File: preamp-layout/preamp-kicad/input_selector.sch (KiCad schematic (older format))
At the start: 40 parts, among them J50 Conn_01x03_Female, J51 Conn_01x03_Male, J52 Conn_01x03_Male, J53 Conn_01x03_Male, J54 Conn_01x03_Male, J55 Conn_01x07_Female, J56 Conn_01x07_Female, J57 Conn_01x03_Male, J58 Conn_01x03_Male, J59 Conn_01x03_Female, J60 Conn_01x02_Male, J61 Conn_01x02_Male, J62 Conn_01x03_Female, J63 Conn_01x03_Female, K2 G6JU, K3 G6JU, K4 G6JU, K5 G6JU, K6 G6JU, K7 G6JU, K8 G6JU, U6 MCP23S17_SP, U7 ULN2003, U8 ULN2003

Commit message: Footprint updates
Footprint creation of relay, ESP32
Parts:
- K2, K3, K4, K5, K6, K7, K8: footprint (none) -> preamp:Relay_DPDT_Omron_G6JU-2P-Y
- U6: footprint Package_DIP:DIP-28_W7.62mm -> Package_SO:SOIC-28W_7.5x17.9mm_P1.27mm
- U7, U8: footprint (none) -> Package_SO:SOIC-16_3.9x9.9mm_P1.27mm
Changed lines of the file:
@@
 F 0 "U8" H 4900 4067 50  0000 C CNN
 F 1 "ULN2003" H 4900 3976 50  0000 C CNN
-F 2 "" H 4950 2850 50  0001 L CNN
+F 2 "Package_SO:SOIC-16_3.9x9.9mm_P1.27mm" H 4950 2850 50  0001 L CNN
 F 3 "http://www.ti.com/lit/ds/symlink/uln2003a.pdf" H 5000 3200 50  0001 C CNN
 	1    4900 3400
@@
 F 0 "U7" H 4900 2267 50  0000 C CNN
 F 1 "ULN2003" H 4900 2176 50  0000 C CNN
-F 2 "" H 4950 1050 50  0001 L CNN
+F 2 "Package_SO:SOIC-16_3.9x9.9mm_P1.27mm" H 4950 1050 50  0001 L CNN
 F 3 "http://www.ti.com/lit/ds/symlink/uln2003a.pdf" H 5000 1400 50  0001 C CNN
 	1    4900 1600
@@
 F 0 "K2" V 10304 1928 50  0000 L CNN
 F 1 "G6JU" V 10395 1928 50  0000 L CNN
-F 2 "" H 10350 1850 50  0001 C CNN
+F 2 "preamp:Relay_DPDT_Omron_G6JU-2P-Y" H 10350 1850 50  0001 C CNN
 F 3 "https://omronfs.omron.com/en_US/ecb/products/pdf/en-g6j.pdf" H 10350 1850 50  0001 C CNN
 	1    10350 1750
@@
 F 0 "K3" V 10304 2928 50  0000 L CNN
 F 1 "G6JU" V 10395 2928 50  0000 L CNN
-F 2 "" H 10350 2850 50  0001 C CNN
+F 2 "preamp:Relay_DPDT_Omron_G6JU-2P-Y" H 10350 2850 50  0001 C CNN
 F 3 "https://omronfs.omron.com/en_US/ecb/products/pdf/en-g6j.pdf" H 10350 2850 50  0001 C CNN
 	1    10350 2750
@@
 F 0 "K4" V 10304 3928 50  0000 L CNN
 F 1 "G6JU" V 10395 3928 50  0000 L CNN
-F 2 "" H 10350 3850 50  0001 C CNN
+F 2 "preamp:Relay_DPDT_Omron_G6JU-2P-Y" H 10350 3850 50  0001 C CNN
 F 3 "https://omronfs.omron.com/en_US/ecb/products/pdf/en-g6j.pdf" H 10350 3850 50  0001 C CNN
 	1    10350 3750
@@
 F 0 "K5" V 10304 4928 50  0000 L CNN
 F 1 "G6JU" V 10395 4928 50  0000 L CNN
-F 2 "" H 10350 4850 50  0001 C CNN
+F 2 "preamp:Relay_DPDT_Omron_G6JU-2P-Y" H 10350 4850 50  0001 C CNN
 F 3 "https://omronfs.omron.com/en_US/ecb/products/pdf/en-g6j.pdf" H 10350 4850 50  0001 C CNN
 	1    10350 4750
@@
 F 0 "K6" V 10304 5928 50  0000 L CNN
 F 1 "G6JU" V 10395 5928 50  0000 L CNN
-F 2 "" H 10350 5850 50  0001 C CNN
+F 2 "preamp:Relay_DPDT_Omron_G6JU-2P-Y" H 10350 5850 50  0001 C CNN
 F 3 "https://omronfs.omron.com/en_US/ecb/products/pdf/en-g6j.pdf" H 10350 5850 50  0001 C CNN
 	1    10350 5750
@@
 F 0 "K7" V 8604 1878 50  0000 L CNN
 F 1 "G6JU" V 8695 1878 50  0000 L CNN
-F 2 "" H 8650 1800 50  0001 C CNN
+F 2 "preamp:Relay_DPDT_Omron_G6JU-2P-Y" H 8650 1800 50  0001 C CNN
 F 3 "https://omronfs.omron.com/en_US/ecb/products/pdf/en-g6j.pdf" H 8650 1800 50  0001 C CNN
 	1    8650 1700
@@
 F 0 "K8" V 8604 2878 50  0000 L CNN
 F 1 "G6JU" V 8695 2878 50  0000 L CNN
-F 2 "" H 8650 2800 50  0001 C CNN
+F 2 "preamp:Relay_DPDT_Omron_G6JU-2P-Y" H 8650 2800 50  0001 C CNN
 F 3 "https://omronfs.omron.com/en_US/ecb/products/pdf/en-g6j.pdf" H 8650 2800 50  0001 C CNN
 	1    8650 2700
@@
 F 0 "K8" H 8550 5727 50  0000 C CNN
 F 1 "G6JU" H 8550 5636 50  0000 C CNN
-F 2 "" H 8550 6050 50  0001 C CNN
+F 2 "preamp:Relay_DPDT_Omron_G6JU-2P-Y" H 8550 6050 50  0001 C CNN
 F 3 "https://omronfs.omron.com/en_US/ecb/products/pdf/en-g6j.pdf" H 8550 6050 50  0001 C CNN
 	3    8550 5950
@@
 F 0 "K8" H 8550 5675 50  0000 C CNN
 F 1 "G6JU" H 8550 5584 50  0000 C CNN
-F 2 "" H 8550 5450 50  0001 C CNN
+F 2 "preamp:Relay_DPDT_Omron_G6JU-2P-Y" H 8550 5450 50  0001 C CNN
 F 3 "https://omronfs.omron.com/en_US/ecb/products/pdf/en-g6j.pdf" H 8550 5450 50  0001 C CNN
 	2    8550 5350
@@
 F 0 "K7" H 8550 4277 50  0000 C CNN
 F 1 "G6JU" H 8550 4186 50  0000 C CNN
-F 2 "" H 8550 4600 50  0001 C CNN
+F 2 "preamp:Relay_DPDT_Omron_G6JU-2P-Y" H 8550 4600 50  0001 C CNN
 F 3 "https://omronfs.omron.com/en_US/ecb/products/pdf/en-g6j.pdf" H 8550 4600 50  0001 C CNN
 	3    8550 4500
@@
 F 0 "K7" H 8550 4225 50  0000 C CNN
 F 1 "G6JU" H 8550 4134 50  0000 C CNN
-F 2 "" H 8550 4000 50  0001 C CNN
+F 2 "preamp:Relay_DPDT_Omron_G6JU-2P-Y" H 8550 4000 50  0001 C CNN
 F 3 "https://omronfs.omron.com/en_US/ecb/products/pdf/en-g6j.pdf" H 8550 4000 50  0001 C CNN
 	2    8550 3900
@@
 F 0 "K2" H 1950 5277 50  0000 C CNN
 F 1 "G6JU" H 1950 5186 50  0000 C CNN
-F 2 "" H 1950 5600 50  0001 C CNN
+F 2 "preamp:Relay_DPDT_Omron_G6JU-2P-Y" H 1950 5600 50  0001 C CNN
 F 3 "https://omronfs.omron.com/en_US/ecb/products/pdf/en-g6j.pdf" H 1950 5600 50  0001 C CNN
 	3    1950 5500
@@
 F 0 "K2" H 1950 5225 50  0000 C CNN
 F 1 "G6JU" H 1950 5134 50  0000 C CNN
-F 2 "" H 1950 5000 50  0001 C CNN
+F 2 "preamp:Relay_DPDT_Omron_G6JU-2P-Y" H 1950 5000 50  0001 C CNN
 F 3 "https://omronfs.omron.com/en_US/ecb/products/pdf/en-g6j.pdf" H 1950 5000 50  0001 C CNN
 	2    1950 4900
@@
 F 0 "K3" H 3750 5277 50  0000 C CNN
 F 1 "G6JU" H 3750 5186 50  0000 C CNN
-F 2 "" H 3750 5600 50  0001 C CNN
+F 2 "preamp:Relay_DPDT_Omron_G6JU-2P-Y" H 3750 5600 50  0001 C CNN
 F 3 "https://omronfs.omron.com/en_US/ecb/products/pdf/en-g6j.pdf" H 3750 5600 50  0001 C CNN
 	3    3750 5500
@@
 F 0 "K3" H 3750 5225 50  0000 C CNN
 F 1 "G6JU" H 3750 5134 50  0000 C CNN
-F 2 "" H 3750 5000 50  0001 C CNN
+F 2 "preamp:Relay_DPDT_Omron_G6JU-2P-Y" H 3750 5000 50  0001 C CNN
 F 3 "https://omronfs.omron.com/en_US/ecb/products/pdf/en-g6j.pdf" H 3750 5000 50  0001 C CNN
 	2    3750 4900
@@
 F 0 "K4" H 1950 6927 50  0000 C CNN
 F 1 "G6JU" H 1950 6836 50  0000 C CNN
-F 2 "" H 1950 7250 50  0001 C CNN
+F 2 "preamp:Relay_DPDT_Omron_G6JU-2P-Y" H 1950 7250 50  0001 C CNN
 F 3 "https://omronfs.omron.com/en_US/ecb/products/pdf/en-g6j.pdf" H 1950 7250 50  0001 C CNN
 	3    1950 7150
@@
 F 0 "K5" H 3750 6927 50  0000 C CNN
 F 1 "G6JU" H 3750 6836 50  0000 C CNN
-F 2 "" H 3750 7250 50  0001 C CNN
+F 2 "preamp:Relay_DPDT_Omron_G6JU-2P-Y" H 3750 7250 50  0001 C CNN
 F 3 "https://omronfs.omron.com/en_US/ecb/products/pdf/en-g6j.pdf" H 3750 7250 50  0001 C CNN
 	3    3750 7150
@@
 F 0 "K5" H 3750 6875 50  0000 C CNN
 F 1 "G6JU" H 3750 6784 50  0000 C CNN
-F 2 "" H 3750 6650 50  0001 C CNN
+F 2 "preamp:Relay_DPDT_Omron_G6JU-2P-Y" H 3750 6650 50  0001 C CNN
 F 3 "https://omronfs.omron.com/en_US/ecb/products/pdf/en-g6j.pdf" H 3750 6650 50  0001 C CNN
 	2    3750 6550
@@
 F 0 "K6" H 5550 6927 50  0000 C CNN
 F 1 "G6JU" H 5550 6836 50  0000 C CNN
-F 2 "" H 5550 7250 50  0001 C CNN
+F 2 "preamp:Relay_DPDT_Omron_G6JU-2P-Y" H 5550 7250 50  0001 C CNN
 F 3 "https://omronfs.omron.com/en_US/ecb/products/pdf/en-g6j.pdf" H 5550 7250 50  0001 C CNN
 	3    5550 7150
@@
 F 0 "K6" H 5550 6875 50  0000 C CNN
 F 1 "G6JU" H 5550 6784 50  0000 C CNN
-F 2 "" H 5550 6650 50  0001 C CNN
+F 2 "preamp:Relay_DPDT_Omron_G6JU-2P-Y" H 5550 6650 50  0001 C CNN
 F 3 "https://omronfs.omron.com/en_US/ecb/products/pdf/en-g6j.pdf" H 5550 6650 50  0001 C CNN
 	2    5550 6550
@@
 F 0 "K4" H 1950 6875 50  0000 C CNN
 F 1 "G6JU" H 1950 6784 50  0000 C CNN
-F 2 "" H 1950 6650 50  0001 C CNN
+F 2 "preamp:Relay_DPDT_Omron_G6JU-2P-Y" H 1950 6650 50  0001 C CNN
 F 3 "https://omronfs.omron.com/en_US/ecb/products/pdf/en-g6j.pdf" H 1950 6650 50  0001 C CNN
 	2    1950 6550
@@
 F 0 "U6" H 2500 3800 50  0000 C CNN
 F 1 "MCP23S17_SP" H 2500 3700 50  0000 C CNN
-F 2 "Package_DIP:DIP-28_W7.62mm" H 2400 1700 50  0001 L CNN
+F 2 "Package_SO:SOIC-28W_7.5x17.9mm_P1.27mm" H 2400 1700 50  0001 L CNN
 F 3 "http://ww1.microchip.com/downloads/en/DeviceDoc/20001952C.pdf" H 2400 1600 50  0001 L CNN
 	1    2200 2700
@@
 P 7000 3150
 AR Path="/6009D432/60248FFE" Ref="#PWR?"  Part="1"
-AR Path="/5E2D8DA2/60248FFE" Ref="#PWR?"  Part="1"
-F 0 "#PWR?" H 7000 2900 50  0001 C CNN
+AR Path="/5E2D8DA2/60248FFE" Ref="#PWR0101"  Part="1"
+F 0 "#PWR0101" H 7000 2900 50  0001 C CNN
 F 1 "GND" H 7005 2977 50  0000 C CNN
 F 2 "" H 7000 3150 50  0001 C CNN

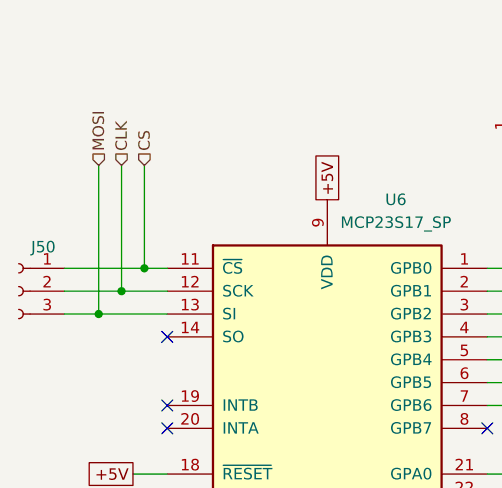
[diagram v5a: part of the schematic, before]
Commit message: Conn / Pin Updates
Updated cable headers, pin names, MCU conn layout. MCP4902 changeout for custom symbol.
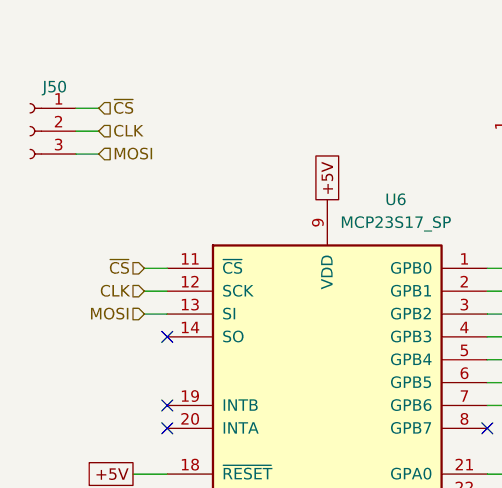
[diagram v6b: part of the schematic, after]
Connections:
- net CS renamed ~CS
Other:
- moved on the sheet: J50
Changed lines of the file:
@@
 Wire Wire Line
 	7000 2050 7000 2150
-Text HLabel 1300 1450 1    50   Input ~ 0
+Text HLabel 1400 2000 0    50   Input ~ 0
 CLK
-Text HLabel 1400 1450 1    50   Input ~ 0
-CS
-Text HLabel 1200 1450 1    50   Input ~ 0
+Text HLabel 1400 1900 0    50   Input ~ 0
+~CS
+Text HLabel 1400 2100 0    50   Input ~ 0
 MOSI
-Wire Wire Line
-	1050 1900 1400 1900
-Wire Wire Line
-	1050 2100 1200 2100
-Wire Wire Line
-	1200 1450 1200 2100
 Text Label 5550 1900 0    50   ~ 0
 IN_3_R+
@@
 L Connector:Conn_01x03_Female J?
 U 1 1 6152C395
-P 850 2000
+P 900 1300
 AR Path="/5E607732/6152C395" Ref="J?"  Part="1"
 AR Path="/5E2D8DA2/6152C395" Ref="J50"  Part="1"
-F 0 "J50" H 742 2193 50  0000 C CNN
-F 1 "Conn_01x03_Female" H 878 1935 50  0001 L CNN
-F 2 "Connector_PinHeader_2.54mm:PinHeader_1x03_P2.54mm_Vertical" H 850 2000 50  0001 C CNN
-F 3 "~" H 850 2000 50  0001 C CNN
-	1    850  2000
+F 0 "J50" H 792 1493 50  0000 C CNN
+F 1 "Conn_01x03_Female" H 928 1235 50  0001 L CNN
+F 2 "Connector_PinHeader_2.54mm:PinHeader_1x03_P2.54mm_Vertical" H 900 1300 50  0001 C CNN
+F 3 "~" H 900 1300 50  0001 C CNN
+	1    900  1300
 	-1   0    0    -1
 $EndComp
@@
 	1    0    0    -1
 $EndComp
-Wire Wire Line
-	1050 2000 1300 2000
-Wire Wire Line
-	1300 1450 1300 2000
-Wire Wire Line
-	1400 1450 1400 1900
-Connection ~ 1200 2100
-Connection ~ 1300 2000
-Connection ~ 1400 1900
-Wire Wire Line
-	1400 1900 1500 1900
-Wire Wire Line
-	1200 2100 1500 2100
-Wire Wire Line
-	1300 2000 1500 2000
 Text GLabel 7000 2850 1    50   UnSpc ~ 0
 +5V
@@
 Wire Wire Line
 	7000 2950 6900 2950
+Wire Wire Line
+	1100 1200 1200 1200
+Wire Wire Line
+	1100 1300 1200 1300
+Wire Wire Line
+	1100 1400 1200 1400
+Wire Wire Line
+	1500 1900 1400 1900
+Wire Wire Line
+	1500 2000 1400 2000
+Wire Wire Line
+	1500 2100 1400 2100
+Text HLabel 1200 1300 2    50   Input ~ 0
+CLK
+Text HLabel 1200 1200 2    50   Input ~ 0
+~CS
+Text HLabel 1200 1400 2    50   Input ~ 0
+MOSI
 $EndSCHEMATC

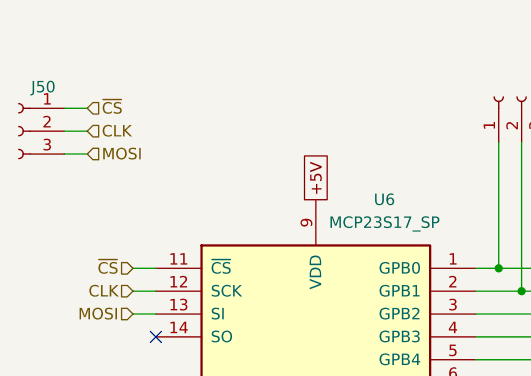
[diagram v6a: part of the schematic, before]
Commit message: Power Supply Update
Grounding made more clear, tied to chassis on AC board. Pins renamed. Aligned with AC wall power convention. General cleanup.
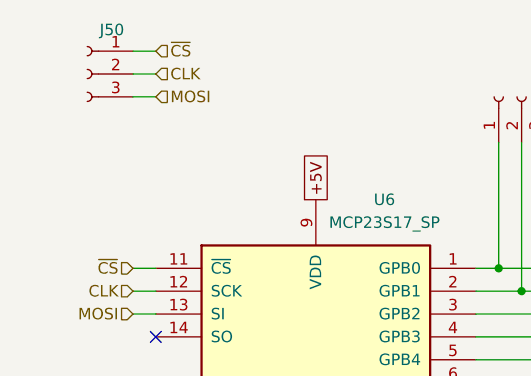
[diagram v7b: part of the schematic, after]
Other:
- moved on the sheet: J50
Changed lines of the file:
@@
 L Connector:Conn_01x03_Female J?
 U 1 1 6152C395
-P 900 1300
+P 1200 1050
 AR Path="/5E607732/6152C395" Ref="J?"  Part="1"
 AR Path="/5E2D8DA2/6152C395" Ref="J50"  Part="1"
-F 0 "J50" H 792 1493 50  0000 C CNN
-F 1 "Conn_01x03_Female" H 928 1235 50  0001 L CNN
-F 2 "Connector_PinHeader_2.54mm:PinHeader_1x03_P2.54mm_Vertical" H 900 1300 50  0001 C CNN
-F 3 "~" H 900 1300 50  0001 C CNN
-	1    900  1300
+F 0 "J50" H 1092 1243 50  0000 C CNN
+F 1 "Conn_01x03_Female" H 1228 985 50  0001 L CNN
+F 2 "Connector_PinHeader_2.54mm:PinHeader_1x03_P2.54mm_Vertical" H 1200 1050 50  0001 C CNN
+F 3 "~" H 1200 1050 50  0001 C CNN
+	1    1200 1050
 	-1   0    0    -1
 $EndComp
@@
 	7000 2950 6900 2950
 Wire Wire Line
-	1100 1200 1200 1200
-Wire Wire Line
-	1100 1300 1200 1300
-Wire Wire Line
-	1100 1400 1200 1400
+	1400 950  1500 950
+Wire Wire Line
+	1400 1050 1500 1050
+Wire Wire Line
+	1400 1150 1500 1150
 Wire Wire Line
 	1500 1900 1400 1900
@@
 Wire Wire Line
 	1500 2100 1400 2100
-Text HLabel 1200 1300 2    50   Input ~ 0
+Text HLabel 1500 1050 2    50   Input ~ 0
 CLK
-Text HLabel 1200 1200 2    50   Input ~ 0
+Text HLabel 1500 950  2    50   Input ~ 0
 ~CS
-Text HLabel 1200 1400 2    50   Input ~ 0
+Text HLabel 1500 1150 2    50   Input ~ 0
 MOSI
 $EndSCHEMATC

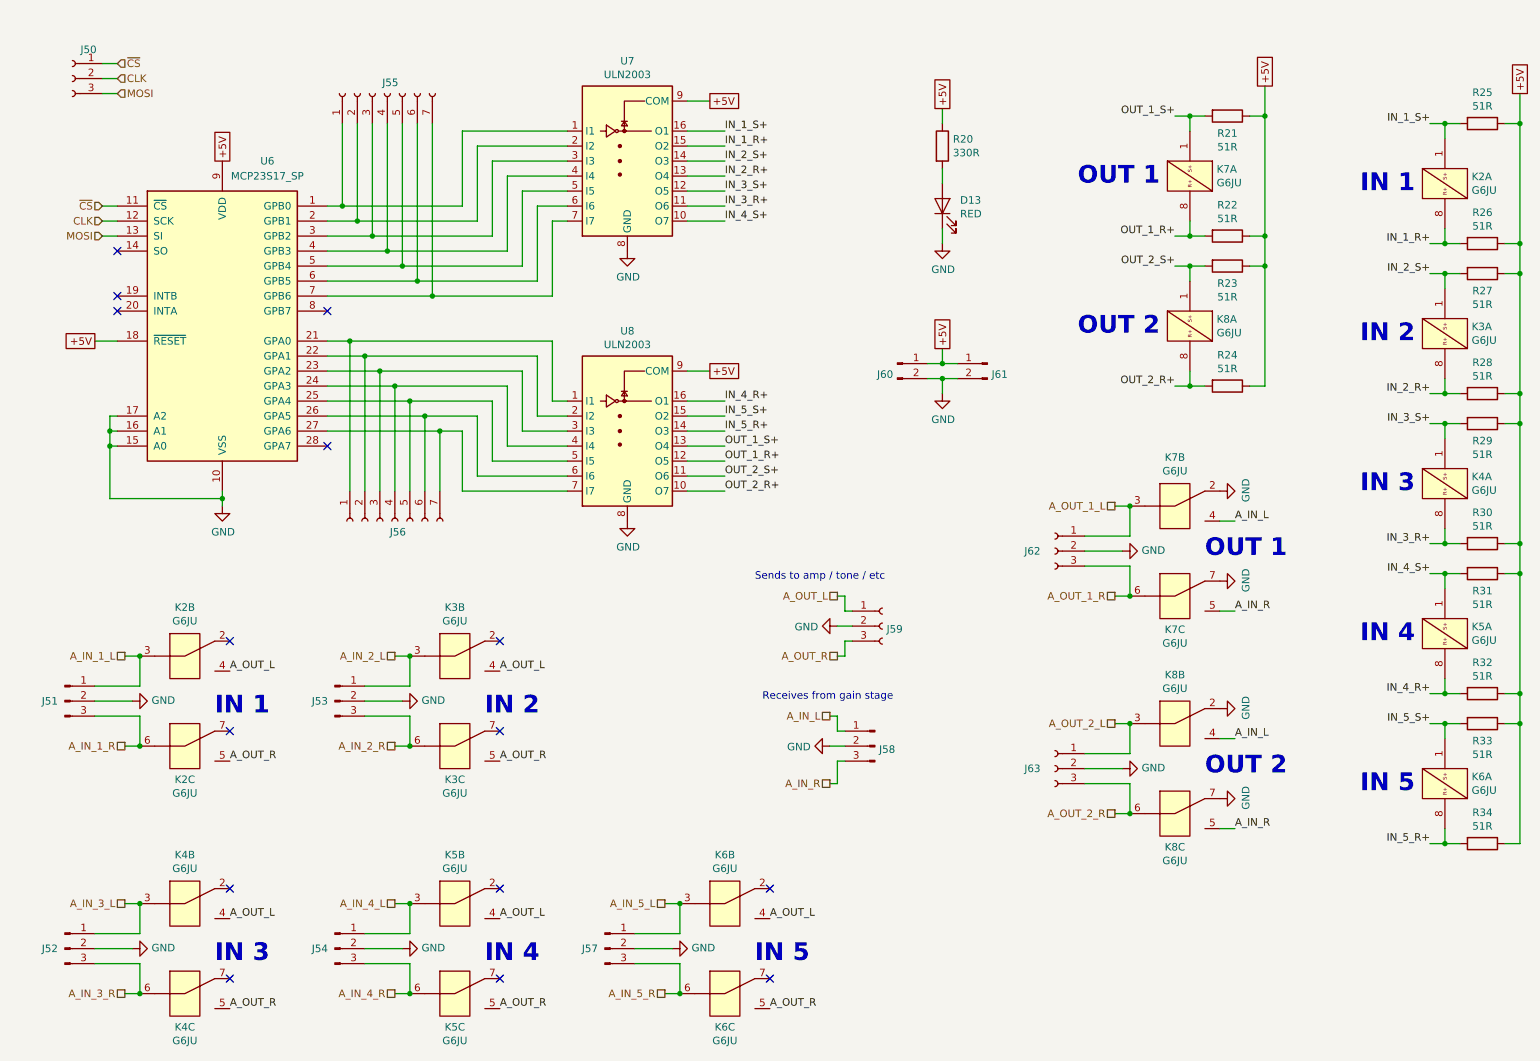
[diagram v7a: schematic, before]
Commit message: Schematic layout updates
schematic optimization. Also implemented encoders with surrounding circuitry (self-contained on encoder board)
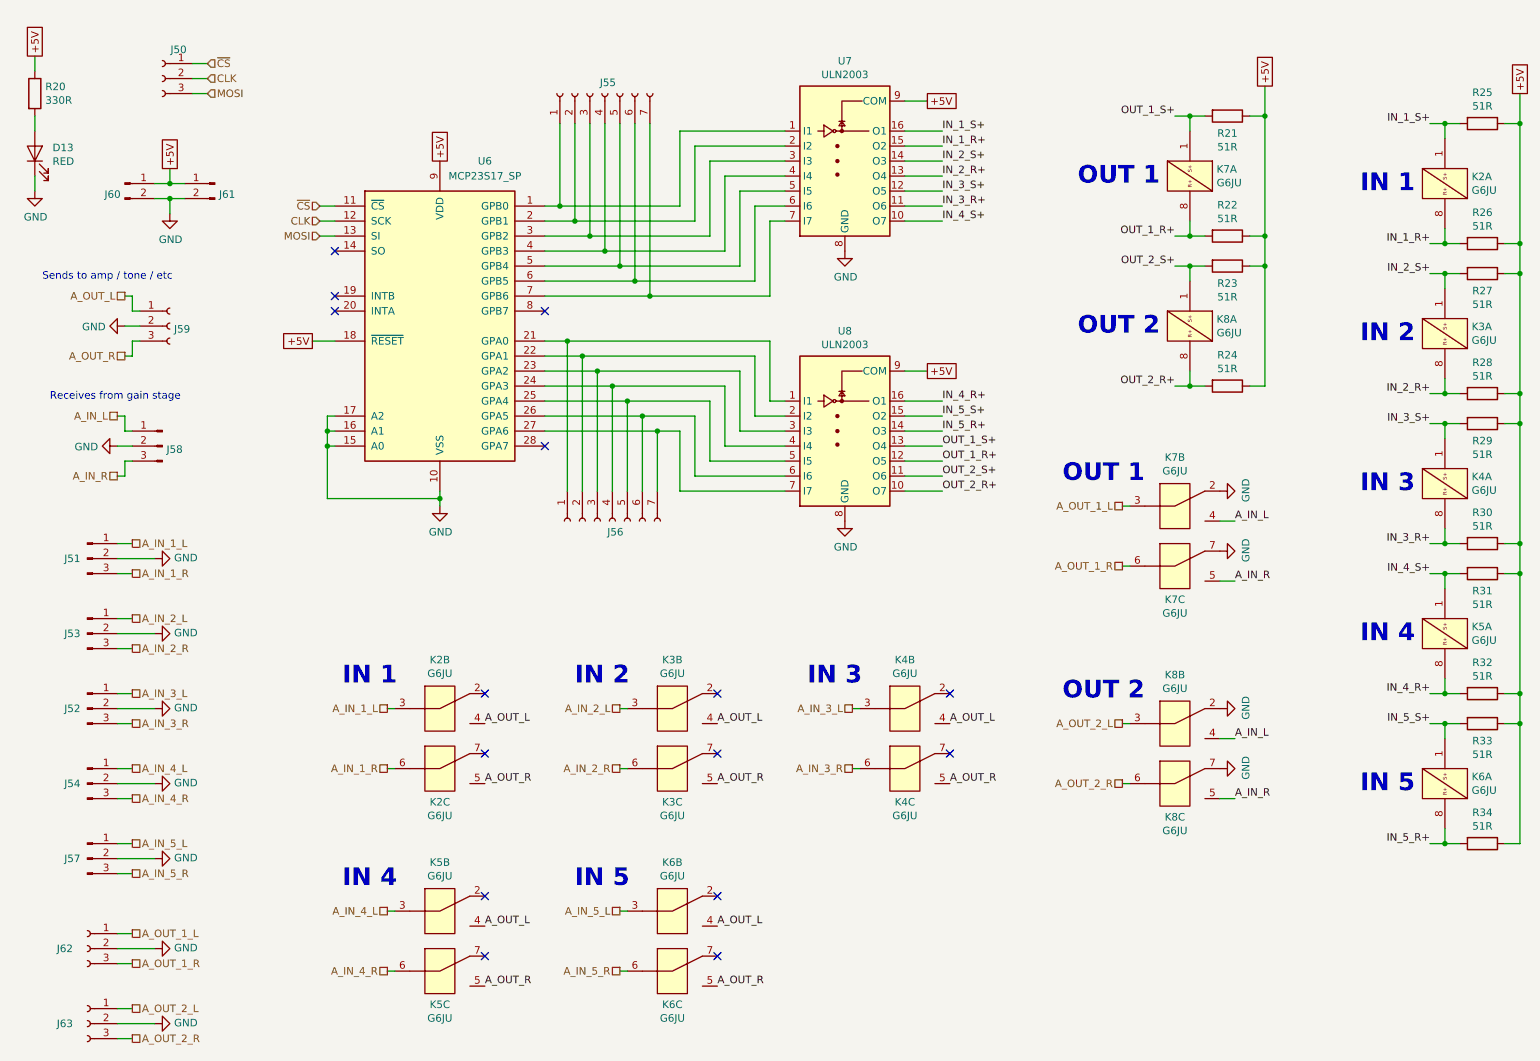
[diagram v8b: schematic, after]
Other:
- moved on the sheet: D13, J50, J51, J52, J53, J54, J55, J56, J57, J58, J59, J60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
